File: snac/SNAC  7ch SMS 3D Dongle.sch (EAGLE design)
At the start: 11 parts, among them IC1 4030D, K2 692112030100, Q9 BC849SMD, X2 STEREOJACK

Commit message: Changed SMS 3D Dongle back to using LV7 on USER IO
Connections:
- net LV1: no longer R20.1
- net LV7: now also R20.1
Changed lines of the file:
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@@
 <label x="73.66" y="190.5" size="1.27" layer="95" xref="yes"/>
-</segment>
-<segment>
-<pinref part="R20" gate="G$1" pin="1"/>
-<wire x1="139.7" y1="165.1" x2="129.54" y2="165.1" width="0.1524" layer="91"/>
-<label x="134.62" y="165.1" size="1.778" layer="95" rot="MR0"/>
 </segment>
 </net>
@@
 <wire x1="68.58" y1="187.96" x2="73.66" y2="187.96" width="0.1524" layer="91"/>
 <label x="73.66" y="187.96" size="1.27" layer="95" xref="yes"/>
+<label x="129.54" y="165.1" size="1.27" layer="95" rot="R180" xref="yes"/>
+</segment>
+<segment>
+<pinref part="R20" gate="G$1" pin="1"/>
+<wire x1="139.7" y1="165.1" x2="129.54" y2="165.1" width="0.1524" layer="91"/>
+<label x="134.62" y="165.1" size="1.778" layer="95" rot="MR0"/>
 </segment>
 </net>

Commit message: SMS 3D and SNES SNAC JST updates
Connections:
- net N$6 renamed TIP
- net N$7 renamed SLEEVE
- net N$8 renamed RING
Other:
- moved on the sheet: C4, R18, X2
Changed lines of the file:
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@@
 <instance part="R17" gate="G$1" x="114.3" y="198.12" rot="R90"/>
 <instance part="C3" gate="G$1" x="127" y="182.88"/>
-<instance part="R18" gate="1" x="139.7" y="198.12" rot="R180"/>
+<instance part="R18" gate="1" x="139.7" y="195.58" rot="R180"/>
 <instance part="Q9" gate="G$1" x="165.1" y="165.1"/>
 <instance part="R19" gate="G$1" x="160.02" y="195.58"/>
 <instance part="R20" gate="G$1" x="144.78" y="165.1"/>
 <instance part="D2" gate="G$1" x="157.48" y="157.48" rot="R90"/>
-<instance part="C4" gate="G$1" x="157.48" y="226.06"/>
-<instance part="X2" gate="1" x="220.98" y="205.74"/>
+<instance part="C4" gate="G$1" x="99.06" y="208.28" rot="R270"/>
+<instance part="X2" gate="1" x="228.6" y="205.74"/>
 <instance part="IC1" gate="P" x="106.68" y="208.28"/>
 </instances>
@@
 <wire x1="116.84" y1="213.36" x2="116.84" y2="226.06" width="0.1524" layer="91"/>
 <junction x="116.84" y="226.06"/>
+<pinref part="IC1" gate="P" pin="VDD"/>
+<wire x1="106.68" y1="215.9" x2="106.68" y2="218.44" width="0.1524" layer="91"/>
+<junction x="106.68" y="226.06"/>
 <pinref part="C4" gate="G$1" pin="1"/>
-<wire x1="149.86" y1="226.06" x2="154.94" y2="226.06" width="0.1524" layer="91"/>
-<junction x="149.86" y="226.06"/>
-<pinref part="IC1" gate="P" pin="VDD"/>
-<wire x1="106.68" y1="215.9" x2="106.68" y2="226.06" width="0.1524" layer="91"/>
-<junction x="106.68" y="226.06"/>
+<wire x1="106.68" y1="218.44" x2="106.68" y2="226.06" width="0.1524" layer="91"/>
+<wire x1="99.06" y1="210.82" x2="99.06" y2="218.44" width="0.1524" layer="91"/>
+<wire x1="99.06" y1="218.44" x2="106.68" y2="218.44" width="0.1524" layer="91"/>
+<junction x="106.68" y="218.44"/>
 </segment>
 </net>
@@
 <label x="73.66" y="200.66" size="1.27" layer="95" xref="yes"/>
 <label x="167.64" y="149.86" size="1.27" layer="95" rot="R270" xref="yes"/>
-<label x="175.26" y="226.06" size="1.27" layer="95" xref="yes"/>
 <label x="106.68" y="187.96" size="1.27" layer="95" rot="R270" xref="yes"/>
 </segment>
@@
 </segment>
 <segment>
-<pinref part="C4" gate="G$1" pin="2"/>
-<wire x1="160.02" y1="226.06" x2="175.26" y2="226.06" width="0.1524" layer="91"/>
-<label x="167.64" y="226.06" size="1.778" layer="95"/>
-</segment>
-<segment>
-<wire x1="106.68" y1="187.96" x2="106.68" y2="200.66" width="0.1524" layer="91"/>
+<wire x1="106.68" y1="187.96" x2="106.68" y2="198.12" width="0.1524" layer="91"/>
 <pinref part="IC1" gate="P" pin="VSS"/>
 <label x="106.68" y="190.5" size="1.778" layer="95" rot="R90"/>
+<pinref part="C4" gate="G$1" pin="2"/>
+<wire x1="106.68" y1="198.12" x2="106.68" y2="200.66" width="0.1524" layer="91"/>
+<wire x1="106.68" y1="198.12" x2="99.06" y2="198.12" width="0.1524" layer="91"/>
+<wire x1="99.06" y1="198.12" x2="99.06" y2="205.74" width="0.1524" layer="91"/>
+<junction x="106.68" y="198.12"/>
 </segment>
 </net>
@@
 <pinref part="R18" gate="1" pin="A"/>
 <wire x1="139.7" y1="210.82" x2="152.4" y2="210.82" width="0.1524" layer="91"/>
-<wire x1="139.7" y1="203.2" x2="139.7" y2="205.74" width="0.1524" layer="91"/>
+<wire x1="139.7" y1="200.66" x2="139.7" y2="203.2" width="0.1524" layer="91"/>
 <junction x="139.7" y="210.82"/>
 <pinref part="R18" gate="1" pin="S"/>
-<wire x1="139.7" y1="205.74" x2="139.7" y2="210.82" width="0.1524" layer="91"/>
-<wire x1="134.62" y1="198.12" x2="134.62" y2="205.74" width="0.1524" layer="91"/>
-<wire x1="134.62" y1="205.74" x2="139.7" y2="205.74" width="0.1524" layer="91"/>
-<junction x="139.7" y="205.74"/>
-</segment>
-</net>
-<net name="N$6" class="0">
+<wire x1="139.7" y1="203.2" x2="139.7" y2="210.82" width="0.1524" layer="91"/>
+<wire x1="134.62" y1="195.58" x2="134.62" y2="203.2" width="0.1524" layer="91"/>
+<wire x1="134.62" y1="203.2" x2="139.7" y2="203.2" width="0.1524" layer="91"/>
+<junction x="139.7" y="203.2"/>
+</segment>
+</net>
+<net name="TIP" class="0">
 <segment>
 <pinref part="IC1" gate="A" pin="O"/>
 <wire x1="167.64" y1="213.36" x2="172.72" y2="213.36" width="0.1524" layer="91"/>
 <pinref part="IC1" gate="C" pin="I0"/>
-<wire x1="172.72" y1="213.36" x2="203.2" y2="213.36" width="0.1524" layer="91"/>
+<wire x1="172.72" y1="213.36" x2="210.82" y2="213.36" width="0.1524" layer="91"/>
 <wire x1="180.34" y1="182.88" x2="172.72" y2="182.88" width="0.1524" layer="91"/>
 <wire x1="172.72" y1="182.88" x2="172.72" y2="200.66" width="0.1524" layer="91"/>
@@
 <junction x="172.72" y="182.88"/>
 <pinref part="X2" gate="1" pin="5"/>
-<wire x1="208.28" y1="208.28" x2="203.2" y2="208.28" width="0.1524" layer="91"/>
-<wire x1="203.2" y1="208.28" x2="203.2" y2="213.36" width="0.1524" layer="91"/>
-</segment>
-</net>
-<net name="N$7" class="0">
+<wire x1="215.9" y1="208.28" x2="210.82" y2="208.28" width="0.1524" layer="91"/>
+<wire x1="210.82" y1="208.28" x2="210.82" y2="213.36" width="0.1524" layer="91"/>
+<label x="198.12" y="213.36" size="1.778" layer="95"/>
+</segment>
+</net>
+<net name="SLEEVE" class="0">
 <segment>
 <pinref part="IC1" gate="B" pin="O"/>
 <pinref part="X2" gate="1" pin="1"/>
-<wire x1="195.58" y1="198.12" x2="208.28" y2="198.12" width="0.1524" layer="91"/>
-</segment>
-</net>
-<net name="N$8" class="0">
+<wire x1="195.58" y1="198.12" x2="215.9" y2="198.12" width="0.1524" layer="91"/>
+<label x="198.12" y="198.12" size="1.778" layer="95"/>
+</segment>
+</net>
+<net name="RING" class="0">
 <segment>
 <pinref part="IC1" gate="C" pin="O"/>
-<wire x1="195.58" y1="180.34" x2="203.2" y2="180.34" width="0.1524" layer="91"/>
-<wire x1="203.2" y1="180.34" x2="203.2" y2="200.66" width="0.1524" layer="91"/>
+<wire x1="195.58" y1="180.34" x2="210.82" y2="180.34" width="0.1524" layer="91"/>
+<wire x1="210.82" y1="180.34" x2="210.82" y2="200.66" width="0.1524" layer="91"/>
 <pinref part="X2" gate="1" pin="2"/>
-<wire x1="203.2" y1="200.66" x2="208.28" y2="200.66" width="0.1524" layer="91"/>
+<wire x1="210.82" y1="200.66" x2="215.9" y2="200.66" width="0.1524" layer="91"/>
+<label x="198.12" y="180.34" size="1.778" layer="95"/>
 </segment>
 </net>
@@
 <pinref part="R17" gate="G$1" pin="1"/>
 <wire x1="124.46" y1="182.88" x2="114.3" y2="182.88" width="0.1524" layer="91"/>
-<wire x1="114.3" y1="182.88" x2="114.3" y2="190.5" width="0.1524" layer="91"/>
+<wire x1="114.3" y1="182.88" x2="114.3" y2="187.96" width="0.1524" layer="91"/>
 <pinref part="R18" gate="1" pin="E"/>
-<wire x1="114.3" y1="190.5" x2="114.3" y2="193.04" width="0.1524" layer="91"/>
-<wire x1="139.7" y1="193.04" x2="139.7" y2="190.5" width="0.1524" layer="91"/>
-<wire x1="139.7" y1="190.5" x2="114.3" y2="190.5" width="0.1524" layer="91"/>
-<junction x="114.3" y="190.5"/>
-</segment>
-</net>
+<wire x1="114.3" y1="187.96" x2="114.3" y2="193.04" width="0.1524" layer="91"/>
+<wire x1="139.7" y1="190.5" x2="139.7" y2="187.96" width="0.1524" layer="91"/>
+<wire x1="139.7" y1="187.96" x2="114.3" y2="187.96" width="0.1524" layer="91"/>
+<junction x="114.3" y="187.96"/>
+</segment>
+</net>

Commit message: changed from LV7 to LV5 pin, for the 3D Glasses boards
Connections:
- net LV5: now also R20.1
- net LV7: no longer R20.1
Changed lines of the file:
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@@
 <wire x1="68.58" y1="195.58" x2="73.66" y2="195.58" width="0.1524" layer="91"/>
 <label x="73.66" y="195.58" size="1.27" layer="95" xref="yes"/>
+<label x="129.54" y="165.1" size="1.27" layer="95" rot="MR0" xref="yes"/>
+</segment>
+<segment>
+<pinref part="R20" gate="G$1" pin="1"/>
+<wire x1="139.7" y1="165.1" x2="129.54" y2="165.1" width="0.1524" layer="91"/>
+<label x="134.62" y="165.1" size="1.778" layer="95" rot="MR0"/>
 </segment>
 </net>
@@
 <wire x1="68.58" y1="187.96" x2="73.66" y2="187.96" width="0.1524" layer="91"/>
 <label x="73.66" y="187.96" size="1.27" layer="95" xref="yes"/>
-<label x="129.54" y="165.1" size="1.27" layer="95" rot="R180" xref="yes"/>
-</segment>
-<segment>
-<pinref part="R20" gate="G$1" pin="1"/>
-<wire x1="139.7" y1="165.1" x2="129.54" y2="165.1" width="0.1524" layer="91"/>
-<label x="134.62" y="165.1" size="1.778" layer="95" rot="MR0"/>
 </segment>
 </net>

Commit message: removed the Compact, TXS chip, and SMS3D with USB3 plug versions
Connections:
- net LV5: no longer R20.1
- net LV6: now also R20.1
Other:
- note added: ""USB 3.0" SKT..."
- note added: "(IOB P6)"
- note added: "(IOB P7)"
- note added: "+3V3"
- note added: "+5V"
- note added: "+9V"
- note added: "1."
- note added: "1. VBUS"
- note added: "15+19. GND"
- note added: "16+18. 5V"
- note added: "17. 3V3"
- note added: "2."
- note added: "2. D-"
- note added: "3."
- note added: "3. D+"
- note added: "4."
- note added: "4. GND"
- note added: "5."
- note added: "5. SSRX-"
- note added: "5V"
- note added: "6."
- note added: "6. SSRX+"
- note added: "7. (via jumper)"
- note added: "7. GND_DRAIN"
- note added: "8. SSTX-"
- note added: "9. SSTX+"
- note added: "<- Older SDRAM board"
- note added: "Arduino_IO0"
- note added: "Arduino_IO1"
- note added: "Arduino_IO10"
- note added: "Arduino_IO11"
- note added: "Arduino_IO12"
- note added: "Arduino_IO13"
- note added: "Arduino_IO14"
- note added: "Arduino_IO15"
- note added: "Arduino_IO2"
- note added: "Arduino_IO3"
- note added: "Arduino_IO4"
- note added: "Arduino_IO5"
- note added: "Arduino_IO6"
- note added: "Arduino_IO7"
- note added: "Arduino_IO8"
- note added: "Arduino_IO9"
- note added: "Arduino_Reset_n"
- note added: "Arduino_VREF"
- note added: "Bliss HDMI..."
- note added: "CKE"
- note added: "CTS"
- note added: "Core name..."
- note added: "DE10 Name..."
- note added: "DH"
- note added: "DIG_MCP_SCL"
- note added: "DIG_MCP_SDA"
- note added: "DIG_SD_CLK"
- note added: "DIG_SD_MISO"
- note added: "DIG_SD_MOSI"
- note added: "DL"
- note added: "DSR"
- note added: "DTR"
- note added: "FPGA PIN..."
- note added: "GND"
- note added: "IO6"
- note added: "IOB NAME..."
- note added: "JP2 PIN1"
- note added: "JP2 PIN10"
- note added: "JP2 PIN2"
- note added: "JP2 PIN3"
- note added: "JP2 PIN4"
- note added: "JP2 PIN5"
- note added: "JP2 PIN6"
- note added: "JP2 PIN7"
- note added: "JP2 PIN8"
- note added: "JP2 PIN9"
- note added: "JP3 PIN1"
- note added: "JP3 PIN2"
- note added: "JP3 PIN3"
- note added: "JP3 PIN4"
- note added: "JP3 PIN5"
- note added: "JP3 PIN6"
- note added: "JP3 PIN7"
- note added: "JP3 PIN8"
- note added: "JP5 PIN1"
- note added: "JP5 PIN2"
- note added: "JP5 PIN3"
- note added: "JP5 PIN4"
- note added: "JP5 PIN5"
- note added: "JP5 PIN6"
- note added: "JP5 PIN7"
- note added: "JP5 PIN8"
- note added: "NC"
- note added: "PIN_AE15"
- note added: "PIN_AF13"
- note added: "PIN_AF15"
- note added: "PIN_AF17"
- note added: "PIN_AG10"
- note added: "PIN_AG11"
- note added: "PIN_AG13"
- note added: "PIN_AG16"
- note added: "PIN_AG8"
- note added: "PIN_AG9"
- note added: "PIN_AH11"
- note added: "PIN_AH12"
- note added: "PIN_AH7"
- note added: "PIN_AH8"
- note added: "PIN_AH9"
- note added: "PIN_U13"
- note added: "PIN_U14"
- note added: "RTS"
- note added: "RX"
- note added: "SOG"
- note added: "TX"
- note added: "USERIO NAME..."
- note added: "USERIO_LV1"
- note added: "USERIO_LV2"
- note added: "USERIO_LV3"
- note added: "USERIO_LV4"
- note added: "USERIO_LV5"
- note added: "USERIO_LV6"
- note added: "USERIO_LV7"
- note added: "USER_IO[0]"
- note added: "USER_IO[1]"
- note added: "USER_IO[2]"
- note added: "USER_IO[3]"
- note added: "USER_IO[4]"
- note added: "USER_IO[5]"
- note added: "USER_IO[6]"

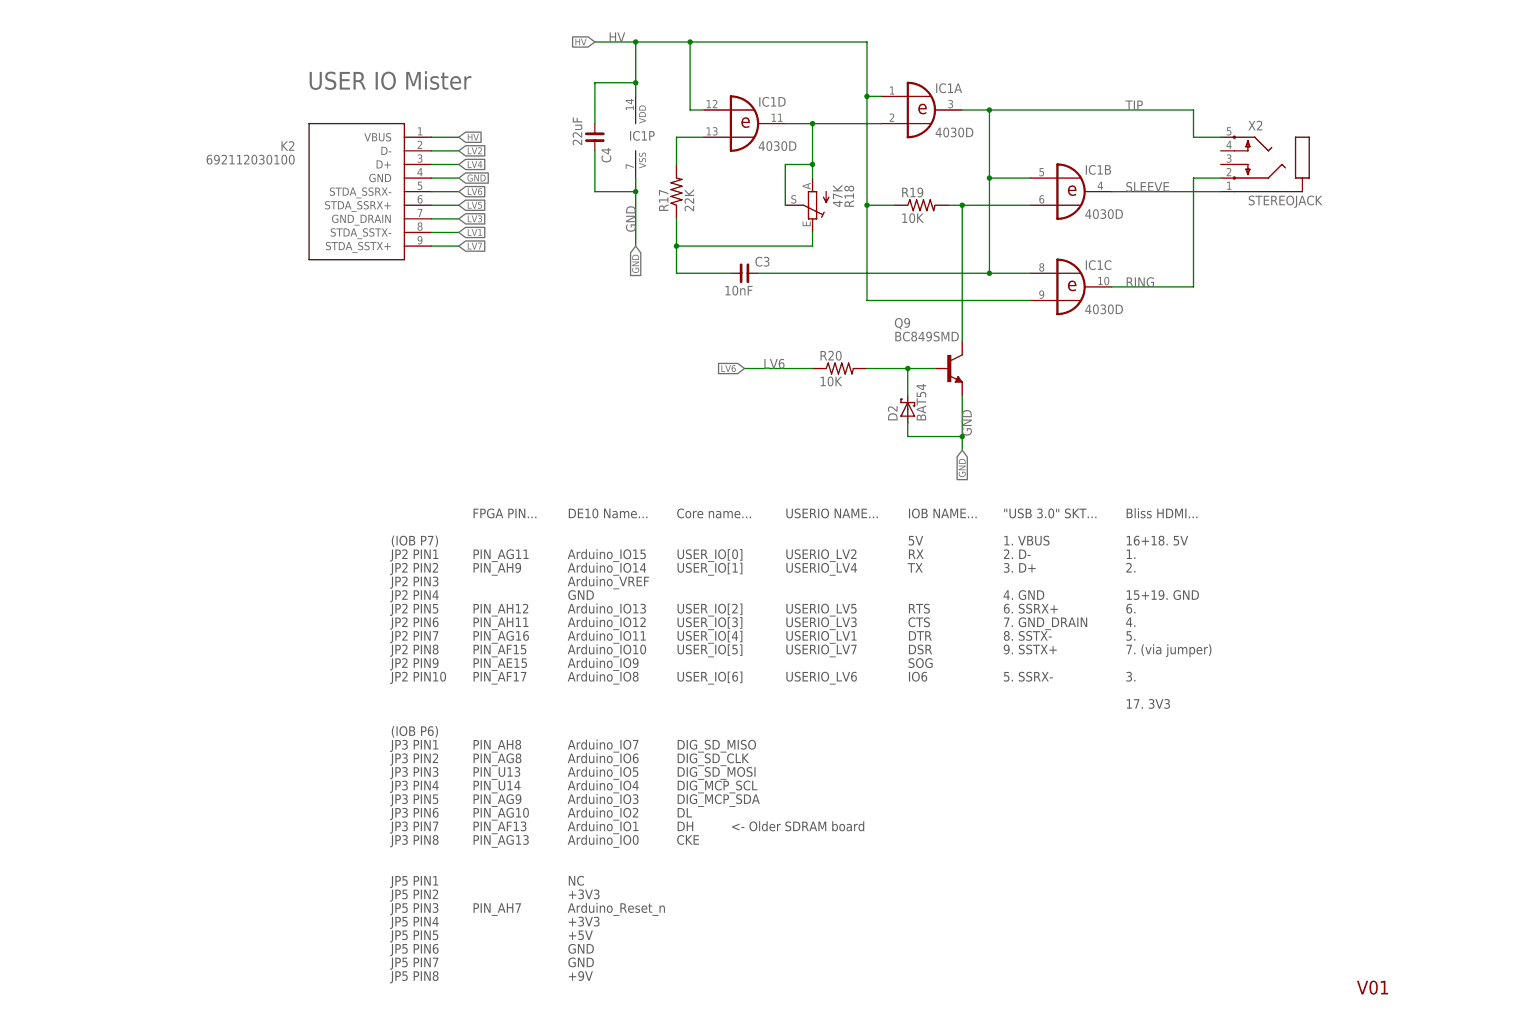
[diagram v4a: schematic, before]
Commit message: Added charge pump to the SMS 3D and SMS DB9 3D PCBs
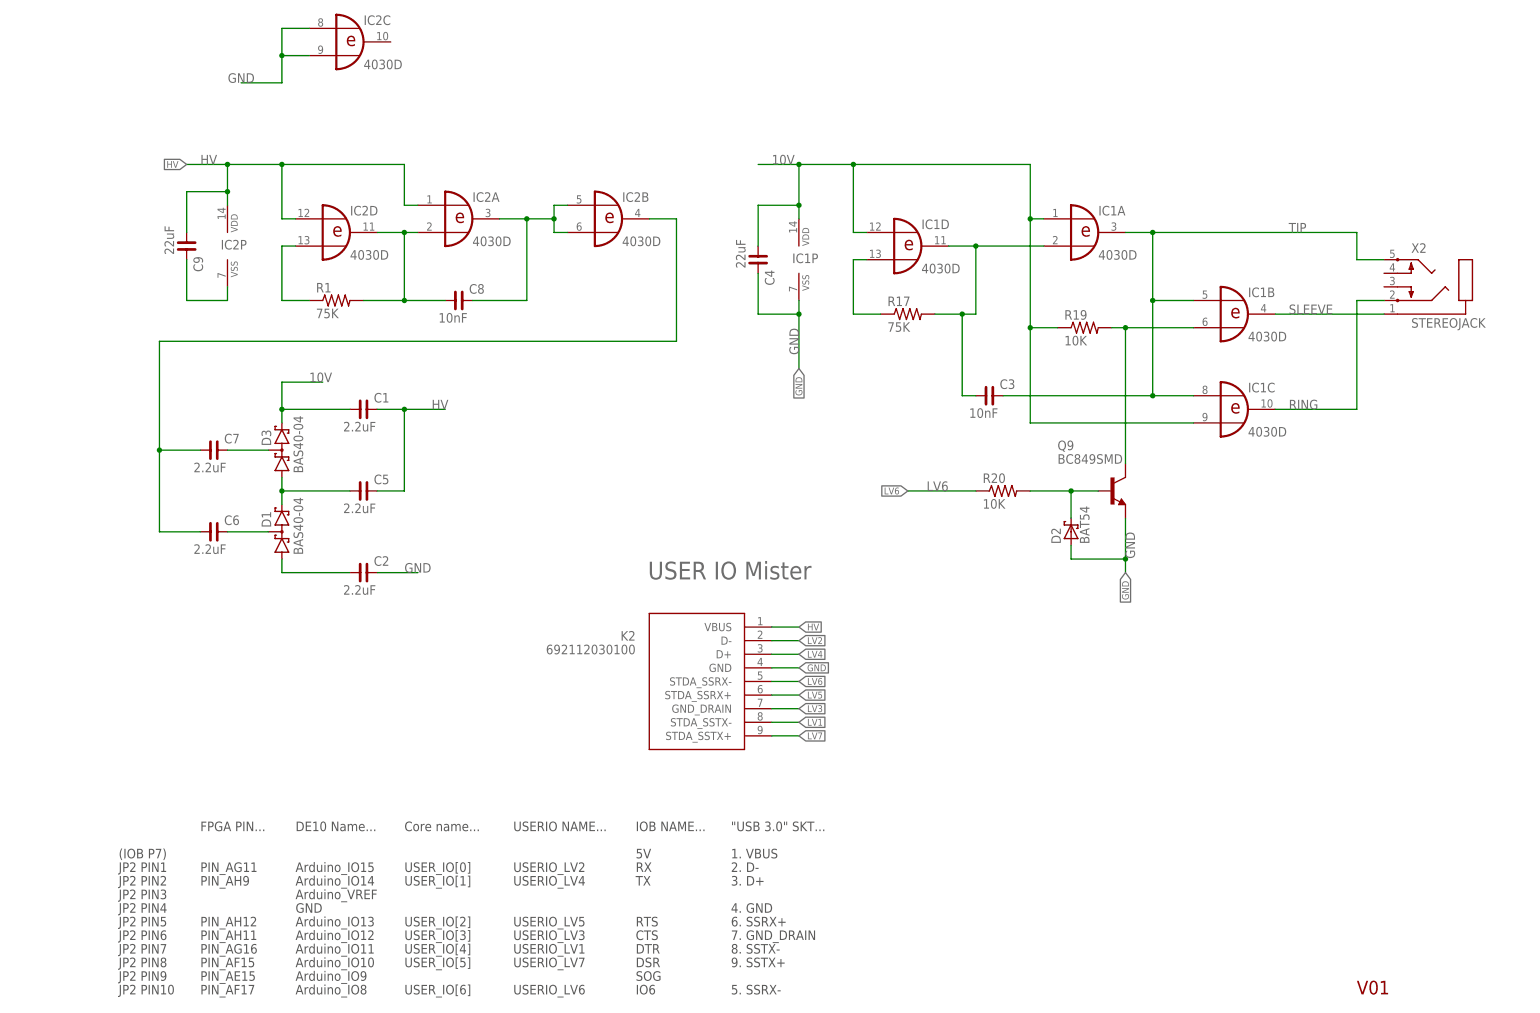
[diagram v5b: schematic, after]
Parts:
- removed R18: 47K, pot:TRIM_EU-B25P
- added C1, C2, C5, C6, C7: 2.2uF, rc-master-smd:C_0805
- added C8: 10nF, rc-master-smd:C_0805
- added C9: 22uF, rc-master-smd:C_0805
- added D1, D3: BAS40-04, diode:BAS40-04
- added IC2: 4030D, 40xx:4030D
- added R1: 75K, SparkFun:RESISTOR0603-RES
- R17: value 22K -> 75K
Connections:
- new net 10V: C1.1, C4.1, D3.C2, IC1A.I0, IC1C.I1, IC1D.I0, IC1P.VDD, R19.1
- new net N$11: C7.2, D3.C1A2
- new net N$12: C6.2, D1.C1A2
- new net N$16: C8.1, IC2A.I1, IC2D.O, R1.2
- new net N$17: IC2D.I1, R1.1
- new net N$6: C5.1, D1.C2, D3.A1
- new net N$7: C6.1, C7.1, IC2B.O
- new net N$8: C2.1, D1.A1
- net GND: now also C2.2, C9.2, IC2C.I0, IC2C.I1, IC2P.VSS
- net HV: now also C1.2, C5.2, C9.1, IC2A.I0, IC2D.I0, IC2P.VDD; no longer C4.1, IC1A.I0, IC1C.I1, IC1D.I0, IC1P.VDD, R19.1
- net N$10: now also R17.1; no longer R17.2
- net N$5: now also C3.1, R17.2; no longer R18.A, R18.S
- net N$9: now also C8.2, IC2A.O, IC2B.I0, IC2B.I1; no longer C3.1, R17.1, R18.E
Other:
- note removed: "(IOB P6)"
- note removed: "+3V3"
- note removed: "+5V"
- note removed: "+9V"
- note removed: "1."
- note removed: "15+19. GND"
- note removed: "16+18. 5V"
- note removed: "17. 3V3"
- note removed: "2."
- note removed: "3."
- note removed: "4."
- note removed: "5."
- note removed: "6."
- note removed: "7. (via jumper)"
- note removed: "<- Older SDRAM board"
- note removed: "Arduino_IO0"
- note removed: "Arduino_IO1"
- note removed: "Arduino_IO2"
- note removed: "Arduino_IO3"
- note removed: "Arduino_IO4"
- note removed: "Arduino_IO5"
- note removed: "Arduino_IO6"
- note removed: "Arduino_IO7"
- note removed: "Arduino_Reset_n"
- note removed: "Bliss HDMI..."
- note removed: "CKE"
- note removed: "DH"
- note removed: "DIG_MCP_SCL"
- note removed: "DIG_MCP_SDA"
- note removed: "DIG_SD_CLK"
- note removed: "DIG_SD_MISO"
- note removed: "DIG_SD_MOSI"
- note removed: "DL"
- note removed: "JP3 PIN1"
- note removed: "JP3 PIN2"
- note removed: "JP3 PIN3"
- note removed: "JP3 PIN4"
- note removed: "JP3 PIN5"
- note removed: "JP3 PIN6"
- note removed: "JP3 PIN7"
- note removed: "JP3 PIN8"
- note removed: "JP5 PIN1"
- note removed: "JP5 PIN2"
- note removed: "JP5 PIN3"
- note removed: "JP5 PIN4"
- note removed: "JP5 PIN5"
- note removed: "JP5 PIN6"
- note removed: "JP5 PIN7"
- note removed: "JP5 PIN8"
- note removed: "NC"
- note removed: "PIN_AF13"
- note removed: "PIN_AG10"
- note removed: "PIN_AG13"
- note removed: "PIN_AG8"
- note removed: "PIN_AG9"
- note removed: "PIN_AH7"
- note removed: "PIN_AH8"
- note removed: "PIN_U13"
- note removed: "PIN_U14"
- moved on the sheet: C3, C4, D2, IC1A, IC1B, IC1C, IC1D, IC1P, K2, Q9, R17, R19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
